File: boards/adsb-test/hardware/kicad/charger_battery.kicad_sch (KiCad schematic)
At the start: 0 parts

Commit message: Release v0.17.0: ADSB_Test power schematics (PD input, 2S charger, rails, monitors)
Co-Authored-By: Claude Opus 5.5 <noreply@anthropic.com>
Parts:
- added C301, C302: 47nF, Capacitor_SMD:C_0402_1005Metric, symbol Device:C
- added C303, C304, C305, C306, C307, C310, C311, C312, C313, C314, C316, C317: 10uF 25V, Capacitor_SMD:C_0805_2012Metric, symbol Device:C
- added C308, C315: 100nF 25V, Capacitor_SMD:C_0402_1005Metric, symbol Device:C
- added C309: 4.7uF 10V, Capacitor_SMD:C_0603_1608Metric, symbol Device:C
- added C318: 1nF 50V, Capacitor_SMD:C_0402_1005Metric, symbol Device:C
- added D301: CHG (amber), LED_SMD:LED_0603_1608Metric, symbol Device:LED
- added J301: 2S Li-ion pack (BAT+, GND, NTC), Connector_JST:JST_XH_B3B-XH-A_1x03_P2.50mm_Vertical, symbol Connector_Generic:Conn_01x03
- added L301: 2.2uH, Inductor_SMD:L_Bourns_SRP7028A_7.3x6.6mm, symbol Device:L
- added R301: 8.2k 1%, Resistor_SMD:R_0402_1005Metric, symbol Device:R
- added R302: 10k, Resistor_SMD:R_0402_1005Metric, symbol Device:R
- added R303: 5.23k 1%, Resistor_SMD:R_0402_1005Metric, symbol Device:R
- added R304: 30.1k 1%, Resistor_SMD:R_0402_1005Metric, symbol Device:R
- added R305: 100R, Resistor_SMD:R_0402_1005Metric, symbol Device:R
- added R306: 2.2k, Resistor_SMD:R_0402_1005Metric, symbol Device:R
- added RS301, RS302: 10m, Resistor_SMD:R_1206_3216Metric, symbol Device:R_Shunt
- added TP301: CHG_QON, TestPoint:TestPoint_Pad_D1.0mm, symbol Connector:TestPoint
- added TP302: BAT_PACK, TestPoint:TestPoint_Pad_D1.0mm, symbol Connector:TestPoint
- added TP303: VSYS, TestPoint:TestPoint_Pad_D1.0mm, symbol Connector:TestPoint
- added TP304: VBUS_CHG, TestPoint:TestPoint_Pad_D1.0mm, symbol Connector:TestPoint
- added U301: BQ25798, Package_DFN_QFN:Texas_RQM0029A_VQFN-29_4x4mm_P0.4mm, symbol Battery_Management:BQ25798
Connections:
- new net BAT_PACK: J301.1 (Pin_1), R305.2, RS301.4, TP302.1
- new net CHG_BATP: R305.1, U301.18 (BATP)
- new net CHG_BTST1: C301.1, U301.4 (BTST1)
- new net CHG_BTST2: C302.1, U301.19 (BTST2)
- new net CHG_CE: R302.1, U301.13 (~{CE})
- new net CHG_LED_A: D301.2 (A), R306.2
- new net CHG_PD_INT: U301.21 (~{INT})
- new net CHG_PMID: C305.1, C306.1, C307.1, C308.1, U301.29 (PMID)
- new net CHG_PROG: R301.1, U301.20 (PROG)
- new net CHG_QON: TP301.1, U301.12 (~{QON})
- new net CHG_REGN: C309.1, R303.1, R306.1, U301.17 (ILIM_HIZ), U301.5 (REGN)
- new net CHG_SDRV: C318.1, U301.24 (SDRV)
- new net CHG_STAT: D301.1 (K), U301.1 (STAT)
- new net CHG_SW1: C301.2, L301.1, U301.28 (SW1)
- new net CHG_SW2: C302.2, L301.2, U301.26 (SW2)
- new net CHG_TS: J301.3 (Pin_3), R303.2, R304.1, U301.16 (TS)
- new net GND: C303.2, C304.2, C305.2, C306.2, C307.2, C308.2, C309.2, C310.2, C311.2, C312.2, C313.2, C314.2, C315.2, C316.2, C317.2, C318.2, J301.2 (Pin_2), R301.2, R302.2, R304.2, U301.10 (ACDRV2), U301.11 (ACDRV1), U301.27 (GND)
- new net I2C_SCL: U301.14 (SCL)
- new net I2C_SDA: U301.15 (SDA)
- new net PM1_CH2_N: RS301.3
- new net PM1_CH2_P: RS301.2
- new net PM1_CH3_N: RS302.3
- new net PM1_CH3_P: RS302.2
- new net VBAT_CHG: C316.1, C317.1, RS301.1, U301.22 (BAT), U301.23 (BAT)
- new net VBUS_CHG: C303.1, C304.1, TP304.1, U301.2 (VBUS), U301.3 (VBUS), U301.8 (VAC2), U301.9 (VAC1)
- new net VSYS: RS302.4, TP303.1
- new net VSYS_CHG: C310.1, C311.1, C312.1, C313.1, C314.1, C315.1, RS302.1, U301.25 (SYS)
- no-connect marks 0 -> 2

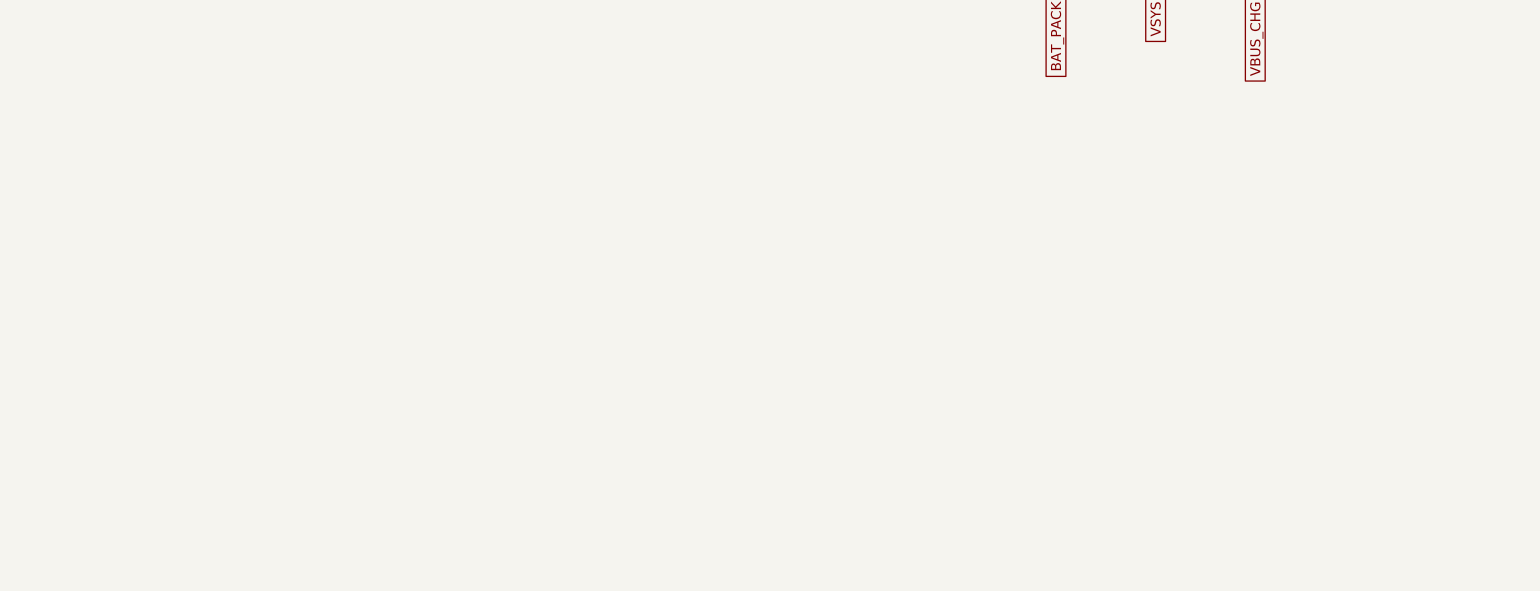
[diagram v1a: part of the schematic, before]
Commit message: Release v0.18.0: power switch, always-on VBACKUP, hand-solder footprints, PCBWay notes
Co-Authored-By: Claude Opus 5.5 <noreply@anthropic.com>
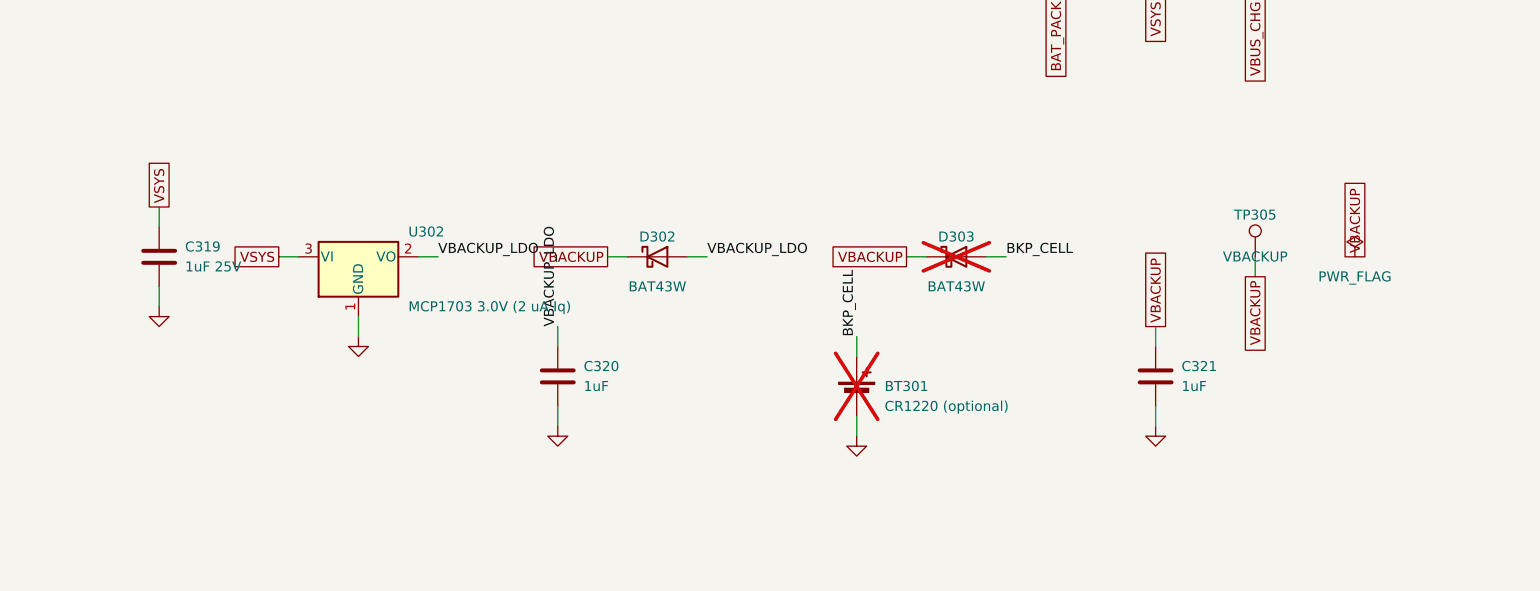
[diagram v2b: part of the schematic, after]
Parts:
- added BT301: CR1220 (optional), Battery:Battery_Panasonic_CR1220-VCN_Vertical_CircularHoles, symbol Device:Battery_Cell
- added C319: 1uF 25V, Capacitor_SMD:C_0805_2012Metric_Pad1.18x1.45mm_HandSolder, symbol Device:C
- added C320, C321: 1uF, Capacitor_SMD:C_0805_2012Metric_Pad1.18x1.45mm_HandSolder, symbol Device:C
- added D302, D303: BAT43W, Diode_SMD:D_SOD-123, symbol Device:D_Schottky
- added TP305: VBACKUP, TestPoint:TestPoint_Pad_D1.5mm, symbol Connector:TestPoint
- added U302: MCP1703 3.0V (2 uA Iq), Package_TO_SOT_SMD:SOT-23, symbol Regulator_Linear:MCP1703Ax-300xxTT
- C301, C302, C308, C315, C318: footprint Capacitor_SMD:C_0402_1005Metric -> Capacitor_SMD:C_0805_2012Metric_Pad1.18x1.45mm_HandSolder
- C303, C304, C305, C306, C307, C310, C311, C312, C313, C314, C316, C317: footprint Capacitor_SMD:C_0805_2012Metric -> Capacitor_SMD:C_0805_2012Metric_Pad1.18x1.45mm_HandSolder
- C309: footprint Capacitor_SMD:C_0603_1608Metric -> Capacitor_SMD:C_0805_2012Metric_Pad1.18x1.45mm_HandSolder
- D301: footprint LED_SMD:LED_0603_1608Metric -> LED_SMD:LED_0805_2012Metric_Pad1.15x1.40mm_HandSolder
- R301, R302, R303, R304, R305, R306: footprint Resistor_SMD:R_0402_1005Metric -> Resistor_SMD:R_0805_2012Metric_Pad1.20x1.40mm_HandSolder
- RS301, RS302: footprint Resistor_SMD:R_1206_3216Metric -> Resistor_SMD:R_1206_3216Metric_Pad1.30x1.75mm_HandSolder
- TP301, TP302, TP303, TP304: footprint TestPoint:TestPoint_Pad_D1.0mm -> TestPoint:TestPoint_Pad_D1.5mm
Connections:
- net GND: now also BT301.2 (-), C319.2, C320.2, C321.2, U302.1 (GND)
- net VSYS: now also C319.1, U302.3 (VI)
- new net BKP_CELL: BT301.1 (+), D303.2 (A)
- new net VBACKUP: C321.1, D302.1 (K), D303.1 (K), TP305.1
- new net VBACKUP_LDO: C320.1, D302.2 (A), U302.2 (VO)

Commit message: Release v0.19.0: hand-solder footprints (m1421, QFNs, SOT-23, SO-8), Rev 1 hand assembly
Co-Authored-By: Claude Opus 5.5 <noreply@anthropic.com>
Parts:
- U302: footprint Package_TO_SOT_SMD:SOT-23 -> Package_TO_SOT_SMD:SOT-23_Handsoldering

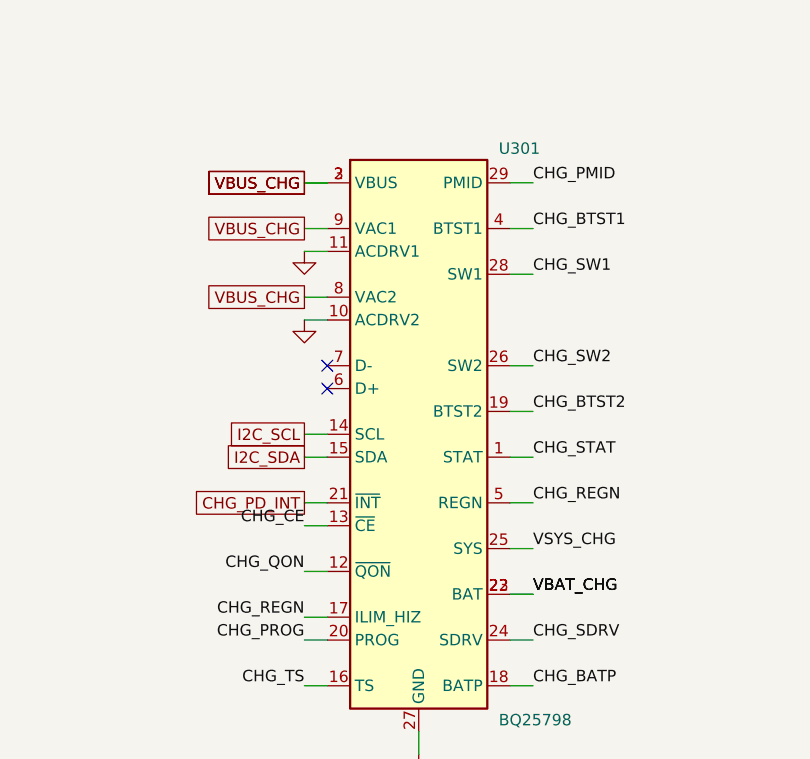
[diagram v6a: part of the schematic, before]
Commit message: Schematic generator: hide stacked pins (KiCad convention) so pin numbers don't overprint
Co-Authored-By: Claude Opus 5.5 <noreply@anthropic.com>
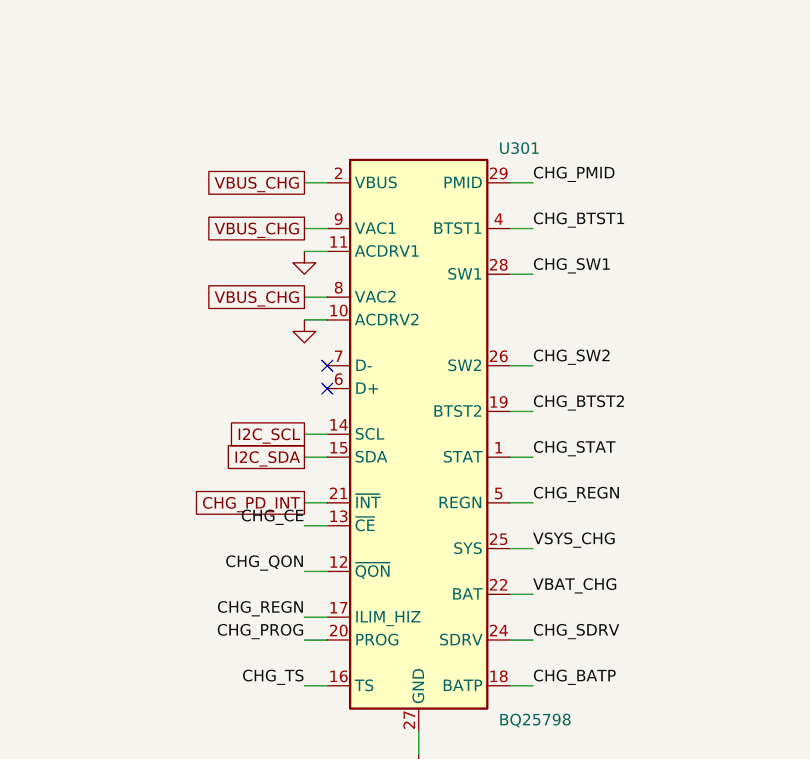
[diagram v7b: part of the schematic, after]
